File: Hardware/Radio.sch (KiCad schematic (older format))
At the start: 15 parts

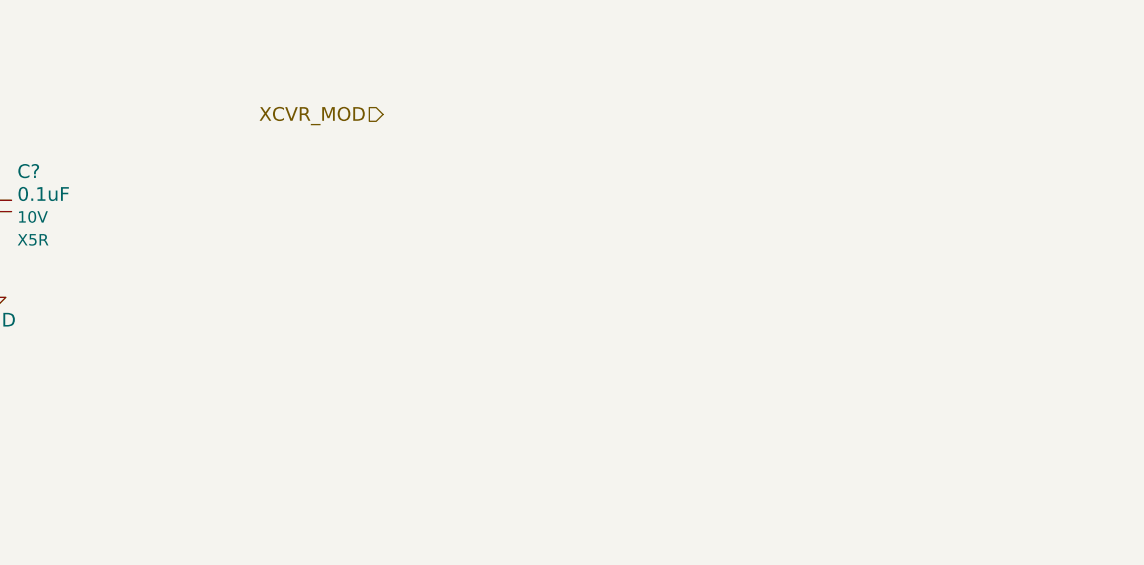
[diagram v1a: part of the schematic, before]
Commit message: Oscillator selection
Closes #35
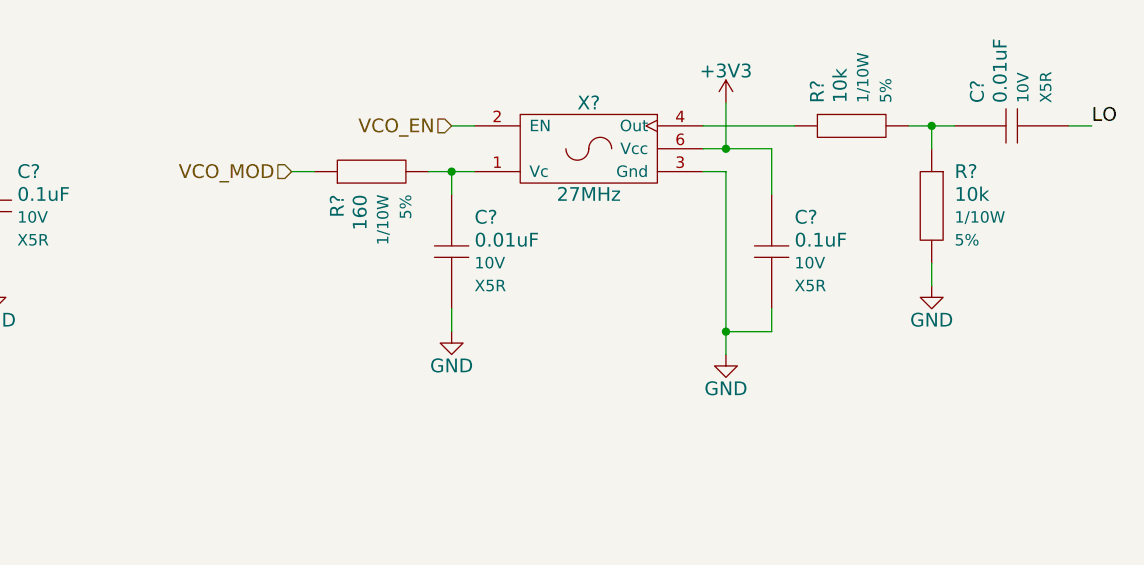
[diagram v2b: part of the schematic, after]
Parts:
- added C?: 0.1uF, symbol Capacitor
- added C? (x2): 0.01uF, symbol Capacitor
- added R? (x2): 10k, symbol Resistor
- added R?: 160, symbol Resistor
- added X?: 27MHz, symbol VCXO
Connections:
- net +3V3: now also C?.1, X?.6 (Vcc)
- net GND: now also C?.2, C?.2, R?.2, X?.3 (Gnd)
- net LO: now also C?.2
- new net: C?.1, R?.2, X?.1 (Vc)
- new net: R?.1, X?.4 (Out)
- new net: C?.1, R?.1, R?.2
- new net VCO_EN: X?.2 (EN)
- new net VCO_MOD: R?.1
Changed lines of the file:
@@
 Wire Wire Line
 	1600 2100 1700 2100
-Text HLabel 7000 1150 0    60   Input ~ 0
-XCVR_MOD
+Text HLabel 6600 1400 0    60   Input ~ 0
+VCO_MOD
 Text Label 2900 1400 0    60   ~ 0
 TXI
@@
 Wire Wire Line
 	2200 3700 2100 3700
+$Comp
+L VCXO X?
+U 1 1 549DAB2F
+P 7900 1300
+F 0 "X?" H 7900 1500 60  0000 C CNN
+F 1 "27MHz" H 7900 1100 60  0000 C CNN
+F 2 "" H 7900 1300 60  0000 C CNN
+F 3 "" H 7900 1300 60  0000 C CNN
+F 4 "CTS" H 7900 1300 60  0001 C CNN "Manufacturer"
+F 5 "357LB3I027M0000" H 7900 1300 60  0001 C CNN "Manufacturer Part #"
+F 6 "Digikey" H 7900 1300 60  0001 C CNN "Vendor"
+F 7 "CTX634CT-ND" H 7900 1300 60  0001 C CNN "Vendor Part #"
+	1    7900 1300
+	1    0    0    -1
+$EndComp
+$Comp
+L Capacitor C?
+U 1 1 549DC500
+P 8700 1750
+F 0 "C?" V 8550 1850 60  0000 L CNN
+F 1 "0.1uF" V 8650 1850 60  0000 L CNN
+F 2 "" H 8600 1750 60  0001 C CNN
+F 3 "" H 8700 1850 60  0001 C CNN
+F 4 "Value" H 8700 1750 60  0001 C CNN "Manufacturer"
+F 5 "Value" H 8700 1750 60  0001 C CNN "Manufacturer Part #"
+F 6 "Value" H 8700 1750 60  0001 C CNN "Vendor"
+F 7 "Value" H 8700 1750 60  0001 C CNN "Vendor Part #"
+F 8 "10V" V 8750 1850 50  0000 L CNN "Voltage"
+F 9 "X5R" V 8850 1850 50  0000 L CNN "Dielectric"
+	1    8700 1750
+	0    1    1    0
+$EndComp
+$Comp
+L GND #PWR?
+U 1 1 549DC55A
+P 8500 2200
+F 0 "#PWR?" H 8500 1950 60  0001 C CNN
+F 1 "GND" H 8500 2050 60  0000 C CNN
+F 2 "" H 8500 2200 60  0000 C CNN
+F 3 "" H 8500 2200 60  0000 C CNN
+	1    8500 2200
+	1    0    0    -1
+$EndComp
+Wire Wire Line
+	8500 1400 8500 2200
+Wire Wire Line
+	8500 1400 8400 1400
+Wire Wire Line
+	8700 2000 8700 2100
+Wire Wire Line
+	8700 2100 8500 2100
+Connection ~ 8500 2100
+$Comp
+L +3V3 #PWR?
+U 1 1 549DC644
+P 8500 1100
+F 0 "#PWR?" H 8500 950 60  0001 C CNN
+F 1 "+3V3" H 8500 1240 60  0000 C CNN
+F 2 "" H 8500 1100 60  0000 C CNN
+F 3 "" H 8500 1100 60  0000 C CNN
+	1    8500 1100
+	1    0    0    -1
+$EndComp
+Wire Wire Line
+	8500 1100 8500 1300
+Wire Wire Line
+	8400 1300 8700 1300
+Wire Wire Line
+	8700 1300 8700 1500
+Connection ~ 8500 1300
+$Comp
+L Resistor R?
+U 1 1 549DC7C7
+P 9050 1200
+F 0 "R?" V 8900 1300 60  0000 L CNN
+F 1 "10k" V 9000 1300 60  0000 L CNN
+F 2 "" H 8950 1200 60  0001 C CNN
+F 3 "" H 9050 1300 60  0001 C CNN
+F 4 "Value" H 9050 1200 60  0001 C CNN "Manufacturer"
+F 5 "Value" H 9050 1200 60  0001 C CNN "Manufacturer Part #"
+F 6 "Value" H 9050 1200 60  0001 C CNN "Vendor"
+F 7 "Value" H 9050 1200 60  0001 C CNN "Vendor Part #"
+F 8 "1/10W" V 9100 1300 50  0000 L CNN "Power"
+F 9 "5%" V 9200 1300 50  0000 L CNN "Tolerance"
+	1    9050 1200
+	1    0    0    -1
+$EndComp
+$Comp
+L Resistor R?
+U 1 1 549DC844
+P 9400 1550
+F 0 "R?" V 9250 1650 60  0000 L CNN
+F 1 "10k" V 9350 1650 60  0000 L CNN
+F 2 "" H 9300 1550 60  0001 C CNN
+F 3 "" H 9400 1650 60  0001 C CNN
+F 4 "Value" H 9400 1550 60  0001 C CNN "Manufacturer"
+F 5 "Value" H 9400 1550 60  0001 C CNN "Manufacturer Part #"
+F 6 "Value" H 9400 1550 60  0001 C CNN "Vendor"
+F 7 "Value" H 9400 1550 60  0001 C CNN "Vendor Part #"
+F 8 "1/10W" V 9450 1650 50  0000 L CNN "Power"
+F 9 "5%" V 9550 1650 50  0000 L CNN "Tolerance"
+	1    9400 1550
+	0    1    1    0
+$EndComp
+$Comp
+L Capacitor C?
+U 1 1 549DC89B
+P 9750 1200
+F 0 "C?" V 9600 1300 60  0000 L CNN
+F 1 "0.01uF" V 9700 1300 60  0000 L CNN
+F 2 "" H 9650 1200 60  0001 C CNN
+F 3 "" H 9750 1300 60  0001 C CNN
+F 4 "Value" H 9750 1200 60  0001 C CNN "Manufacturer"
+F 5 "Value" H 9750 1200 60  0001 C CNN "Manufacturer Part #"
+F 6 "Value" H 9750 1200 60  0001 C CNN "Vendor"
+F 7 "Value" H 9750 1200 60  0001 C CNN "Vendor Part #"
+F 8 "10V" V 9800 1300 50  0000 L CNN "Voltage"
+F 9 "X5R" V 9900 1300 50  0000 L CNN "Dielectric"
+	1    9750 1200
+	1    0    0    -1
+$EndComp
+Text Label 10100 1200 0    60   ~ 0
+LO
+Wire Wire Line
+	10100 1200 10000 1200
+Wire Wire Line
+	8400 1200 8800 1200
+Wire Wire Line
+	9300 1200 9500 1200
+Wire Wire Line
+	9400 1300 9400 1200
+Connection ~ 9400 1200
+$Comp
+L GND #PWR?
+U 1 1 549DCA64
+P 9400 1900
+F 0 "#PWR?" H 9400 1650 60  0001 C CNN
+F 1 "GND" H 9400 1750 60  0000 C CNN
+F 2 "" H 9400 1900 60  0000 C CNN
+F 3 "" H 9400 1900 60  0000 C CNN
+	1    9400 1900
+	1    0    0    -1
+$EndComp
+Wire Wire Line
+	9400 1900 9400 1800
+Text HLabel 7300 1200 0    60   Input ~ 0
+VCO_EN
+Wire Wire Line
+	7300 1200 7400 1200
+$Comp
+L Capacitor C?
+U 1 1 549DD1F3
+P 7300 1750
+F 0 "C?" V 7150 1850 60  0000 L CNN
+F 1 "0.01uF" V 7250 1850 60  0000 L CNN
+F 2 "" H 7200 1750 60  0001 C CNN
+F 3 "" H 7300 1850 60  0001 C CNN
+F 4 "Value" H 7300 1750 60  0001 C CNN "Manufacturer"
+F 5 "Value" H 7300 1750 60  0001 C CNN "Manufacturer Part #"
+F 6 "Value" H 7300 1750 60  0001 C CNN "Vendor"
+F 7 "Value" H 7300 1750 60  0001 C CNN "Vendor Part #"
+F 8 "10V" V 7350 1850 50  0000 L CNN "Voltage"
+F 9 "X5R" V 7450 1850 50  0000 L CNN "Dielectric"
+	1    7300 1750
+	0    1    1    0
+$EndComp
+$Comp
+L Resistor R?
+U 1 1 549DD250
+P 6950 1400
+F 0 "R?" V 6800 1500 60  0000 L CNN
+F 1 "160" V 6900 1500 60  0000 L CNN
+F 2 "" H 6850 1400 60  0001 C CNN
+F 3 "" H 6950 1500 60  0001 C CNN
+F 4 "Value" H 6950 1400 60  0001 C CNN "Manufacturer"
+F 5 "Value" H 6950 1400 60  0001 C CNN "Manufacturer Part #"
+F 6 "Value" H 6950 1400 60  0001 C CNN "Vendor"
+F 7 "Value" H 6950 1400 60  0001 C CNN "Vendor Part #"
+F 8 "1/10W" V 7000 1500 50  0000 L CNN "Power"
+F 9 "5%" V 7100 1500 50  0000 L CNN "Tolerance"
+	1    6950 1400
+	1    0    0    1
+$EndComp
+Wire Wire Line
+	6600 1400 6700 1400
+Wire Wire Line
+	7200 1400 7400 1400
+Wire Wire Line
+	7300 1500 7300 1400
+Connection ~ 7300 1400
+$Comp
+L GND #PWR?
+U 1 1 549DD4D8
+P 7300 2100
+F 0 "#PWR?" H 7300 1850 60  0001 C CNN
+F 1 "GND" H 7300 1950 60  0000 C CNN
+F 2 "" H 7300 2100 60  0000 C CNN
+F 3 "" H 7300 2100 60  0000 C CNN
+	1    7300 2100
+	1    0    0    -1
+$EndComp
+Wire Wire Line
+	7300 2100 7300 2000
 $EndSCHEMATC

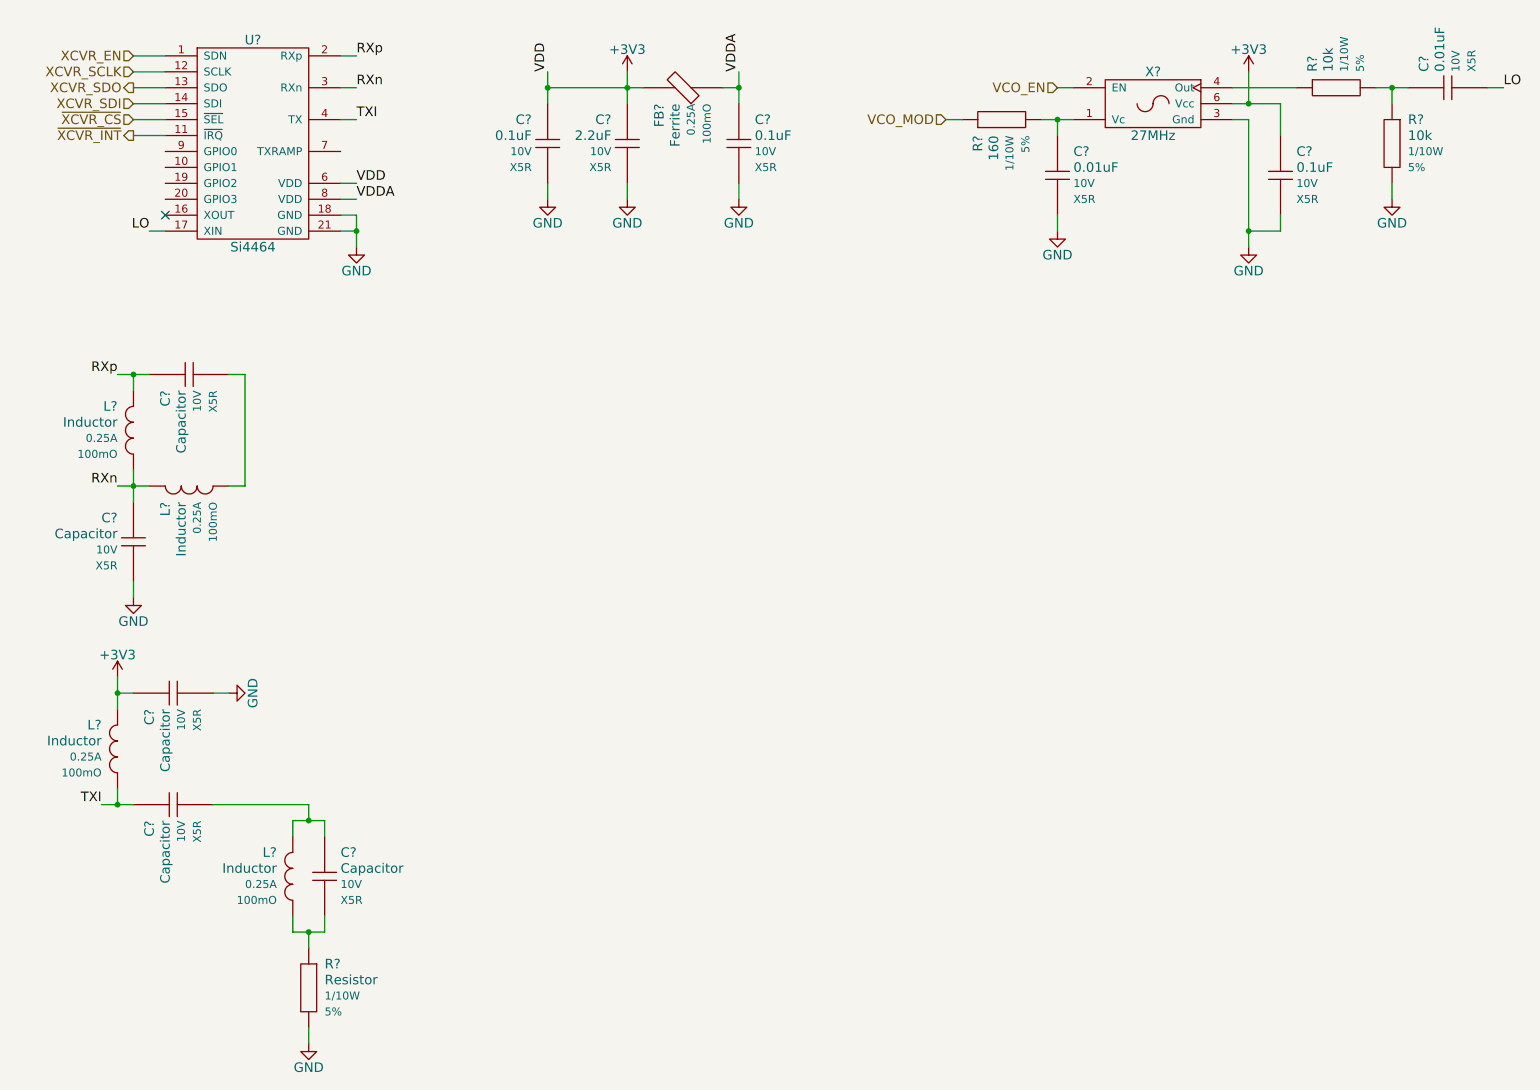
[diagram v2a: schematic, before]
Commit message: Add RF switch
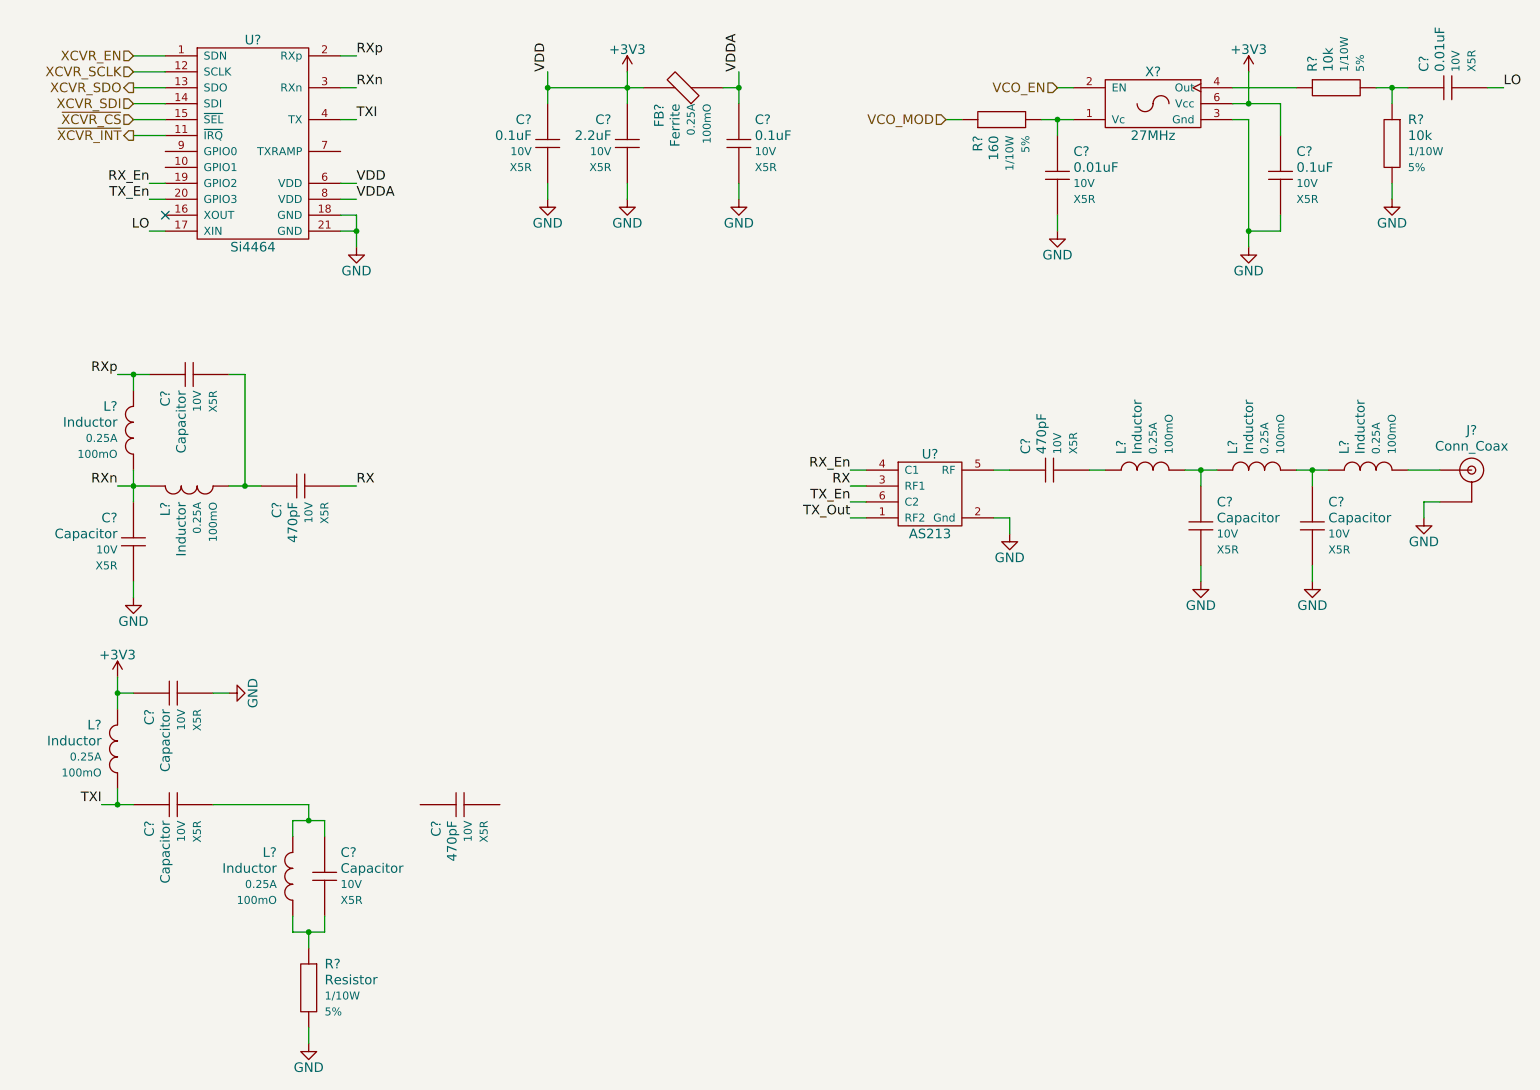
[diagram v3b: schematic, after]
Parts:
- added C? (x3): 470pF, symbol Capacitor
- added C? (x2): Capacitor, symbol Capacitor
- added J?: Conn_Coax, symbol Conn_Coax
- added L? (x3): Inductor, symbol Inductor
- added U?: AS213, symbol AS213
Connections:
- net GND: now also C?.2, C?.2, J?.2, U?.2 (Gnd)
- net RX_En: now reaches U?.19 (GPIO2)
- net RX_En: now also U?.4 (C1)
- net TX_En: now reaches U?.20 (GPIO3)
- net TX_En: now also U?.6 (C2)
- net at C?.2, L?.2: now also C?.1
- new net: C?.1, U?.5 (RF)
- new net: C?.2, L?.1
- new net: C?.1, L?.1, L?.2 (x2)
- new net: J?.1, L?.2
- new net RX: C?.2, U?.3 (RF1)
- new net TX_Out: U?.1 (RF2)

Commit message: Power sheet BOM fields
Remove annotations
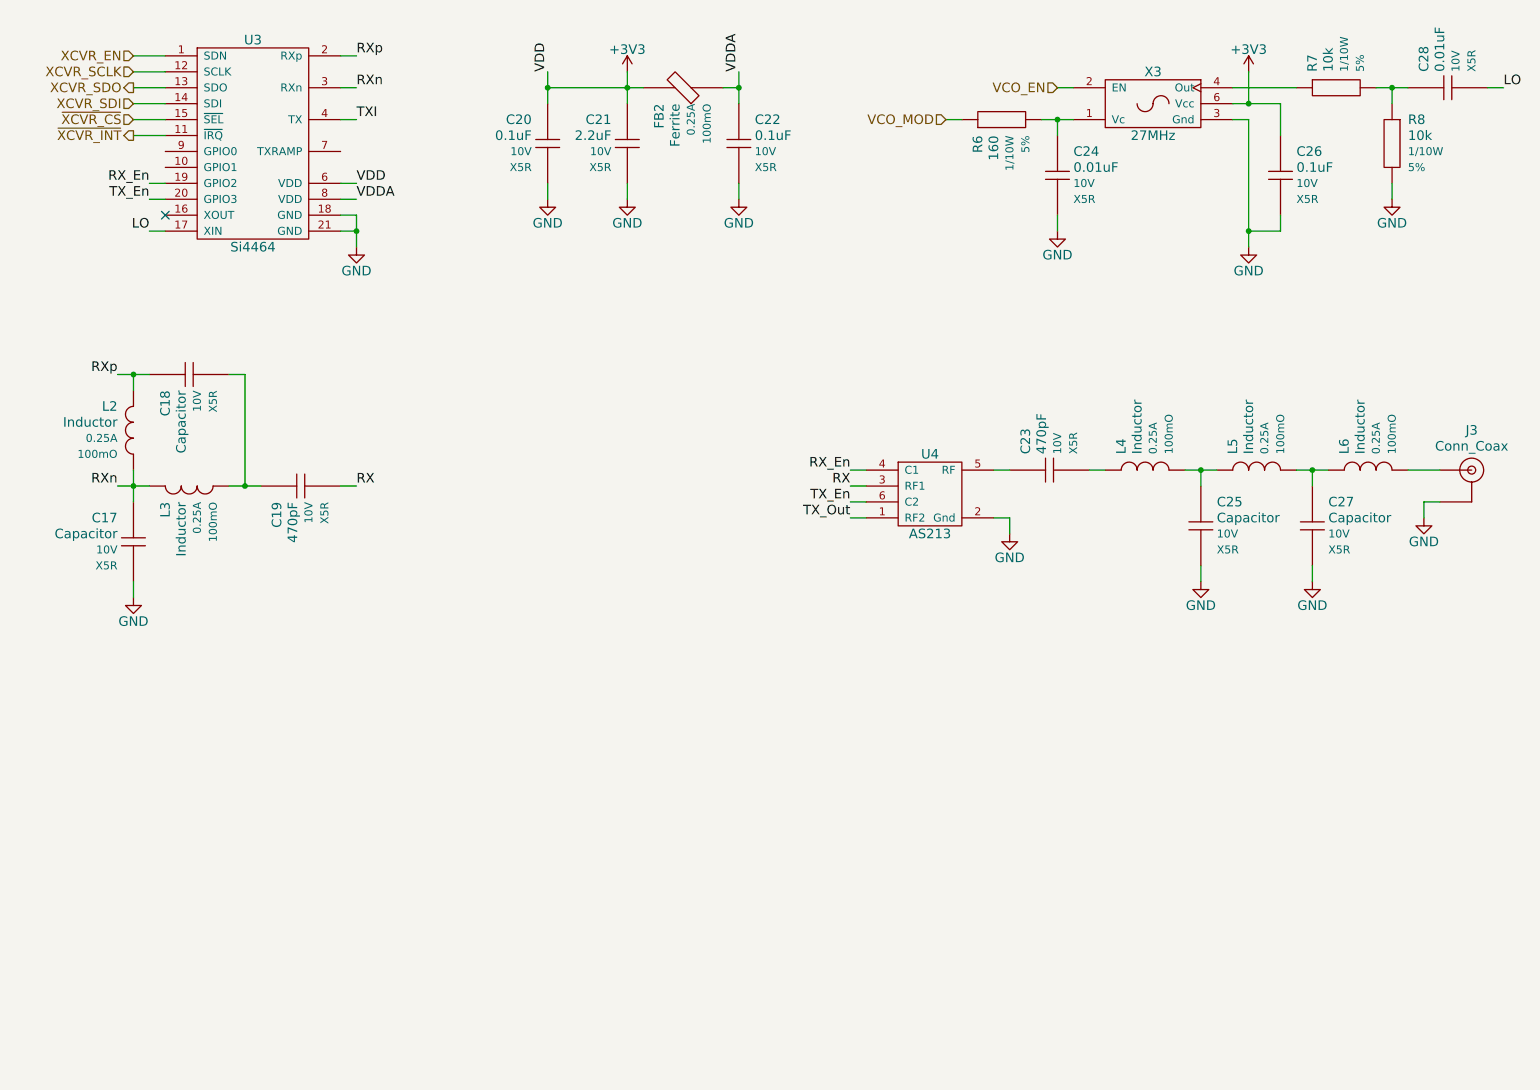
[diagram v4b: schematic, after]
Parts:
- removed C? (x3): Capacitor, symbol Capacitor
- removed C?: 470pF, symbol Capacitor
- removed L? (x2): Inductor, symbol Inductor
- removed R?: Resistor, symbol Resistor
- gave numbers to parts that had none: 25
